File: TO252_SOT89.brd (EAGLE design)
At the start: 5 parts

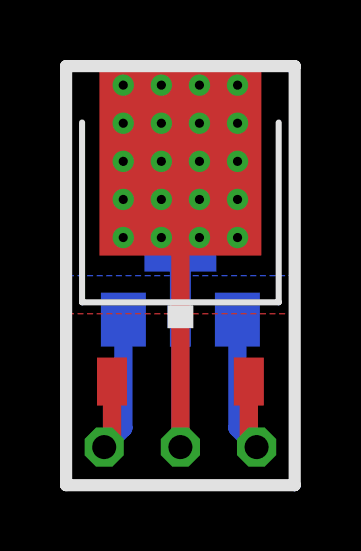
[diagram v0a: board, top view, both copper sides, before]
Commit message: adjusted trace widths
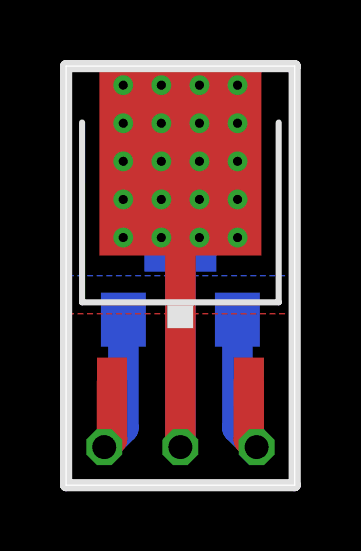
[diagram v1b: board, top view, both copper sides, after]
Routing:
- net S$306: track 19.4 -> 18.8 mm
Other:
- board outline added: 7.6 x 14 mm
